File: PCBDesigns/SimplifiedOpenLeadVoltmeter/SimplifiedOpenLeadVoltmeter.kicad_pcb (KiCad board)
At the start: 4 copper layers, 23.9 x 51.3 mm, 33 parts, among them J14 Barrel_Jack, J2 Conn_01x03_Pin, J3 Conn_01x04_MountingPin, J5 Conn_01x03_Pin, Q8 AO3400A MOSFET, U1 ADuM1200AR, U10 LM4040DBZ-2.5, U13 ISO1540, U14 RFM-0505S, U3 ADS1115IDGS

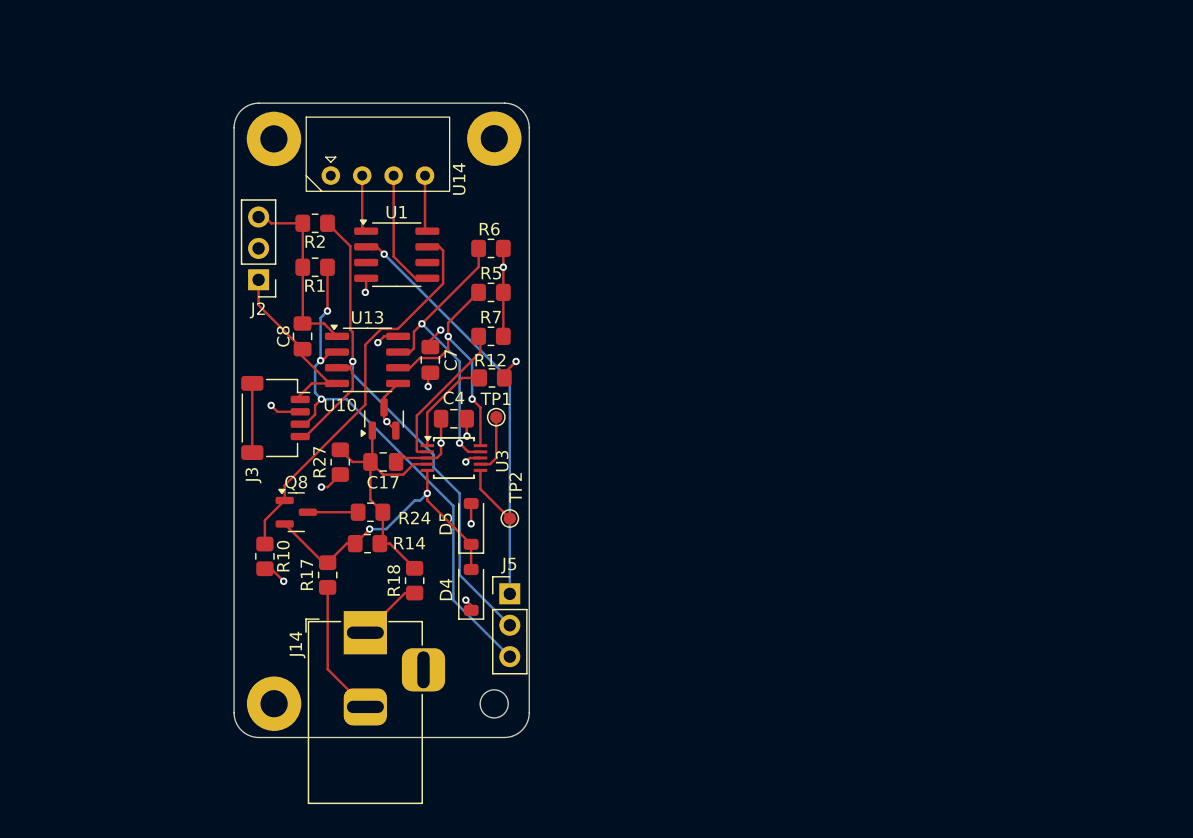
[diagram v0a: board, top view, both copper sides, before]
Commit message: Updates, see description
Updated programming for open lead detect board
worked on various PCBs, including a new open lead voltmeter design with few components
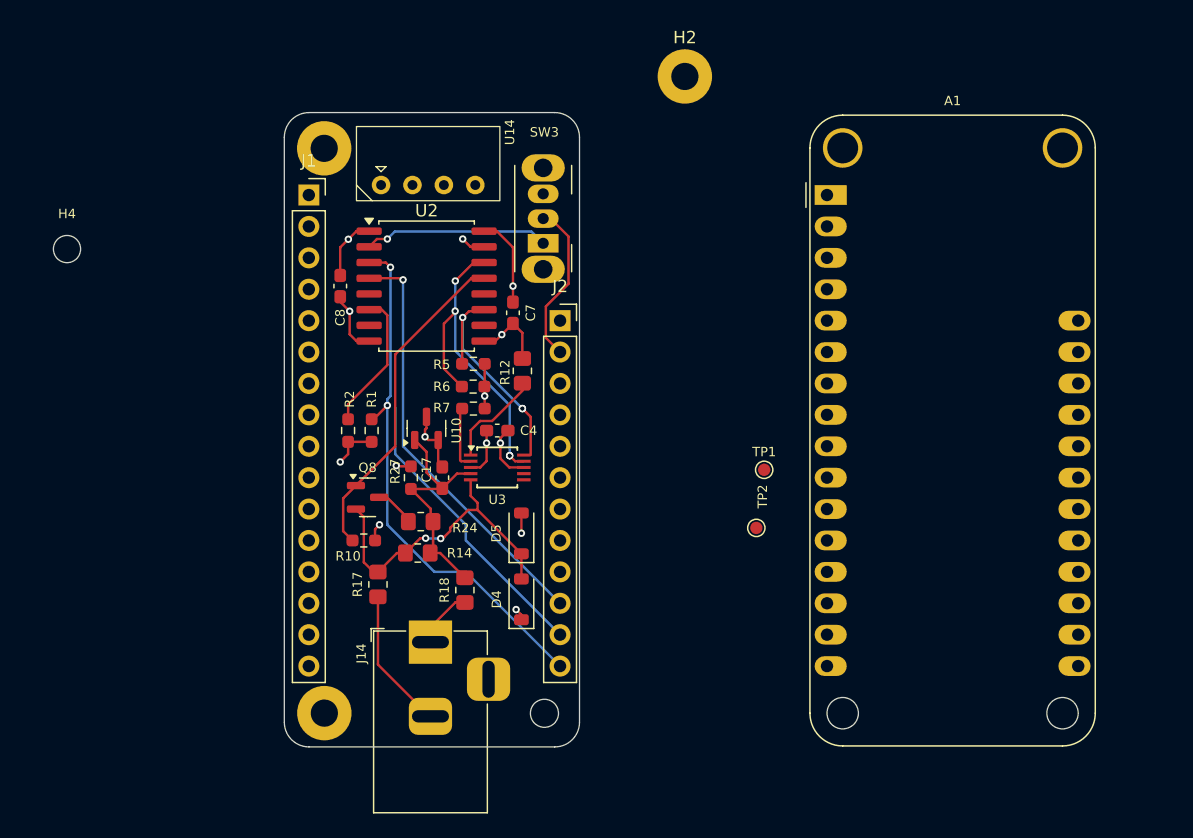
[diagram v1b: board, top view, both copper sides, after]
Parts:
- removed J3: Conn_01x04_MountingPin, Connector_JST:JST_SH_SM04B-SRSS-TB_1x04-1MP_P1.00mm_Horizontal
- removed J5: Conn_01x03_Pin, Connector_PinHeader_2.54mm:PinHeader_1x03_P2.54mm_Vertical
- removed U1: ADuM1200AR, Package_SO:SOIC-8_3.9x4.9mm_P1.27mm
- removed U13: ISO1540, Package_SO:SOIC-8_3.9x4.9mm_P1.27mm
- added A1: Adafruit_Feather_32u4_BluefruitLE, Module:Adafruit_Feather_WithMountingHoles, F.Cu at (194.3, 67.3)
- added H4: MountingHole, MountingHole:MountingHole_2.2mm_M2_ISO14580, F.Cu at (132.8, 71.7)
- added J1: Conn_01x16_Pin, Connector_PinSocket_2.54mm:PinSocket_1x16_P2.54mm_Vertical, F.Cu at (152.4, 67.3)
- added SW3: SW_SPDT, Button_Switch_THT:SW_Slide_SPDT_Angled_CK_OS102011MA1Q, F.Cu at (171.4, 71.2)
- added U2: ISO1644DWR, Package_SO:SOIC-16W_7.5x10.3mm_P1.27mm, F.Cu at (161.9, 74.7)
- C17, C4, C7, C8: footprint Capacitor_SMD:C_0805_2012Metric_Pad1.18x1.45mm_HandSolder -> Capacitor_SMD:C_0603_1608Metric_Pad1.08x0.95mm_HandSolder
- J2: value Conn_01x03_Pin -> Conn_01x12_Pin; footprint Connector_PinHeader_2.54mm:PinHeader_1x03_P2.54mm_Vertical -> Connector_PinSocket_2.54mm:PinSocket_1x12_P2.54mm_Vertical
- R1, R10, R2, R27, R5, R6, R7: footprint Resistor_SMD:R_0805_2012Metric_Pad1.20x1.40mm_HandSolder -> Resistor_SMD:R_0603_1608Metric_Pad0.98x0.95mm_HandSolder
- U14: value RFM-0505S -> DC-DC 0305
- moved J2 24.6 mm to (172.7, 77.5), turned to 0 degrees
- moved TP1 22.1 mm to (189.2, 89.5)
- moved TP2 20.0 mm to (188.6, 94.2)
- moved R2 17.0 mm to (155.6, 86.4), turned to 90 degrees
- moved H2 16.2 mm to (182.8, 57.7)
- moved R1 14.0 mm to (157.5, 86.4), turned to 90 degrees
- moved R6 11.3 mm to (165.7, 82.8)
- moved R10 8.10 mm to (156.8, 95.2), turned to 180 degrees
- moved C7 7.69 mm to (168.9, 76.8)
- moved R7 6.01 mm to (165.7, 84.6)
- moved R5 5.95 mm to (165.7, 81.0)
- moved Q8 5.89 mm to (157.1, 91.8)
- moved R27 5.85 mm to (160.7, 90.2), turned to -90 degrees
- moved J14 5.32 mm to (162.2, 103.5)
- moved C8 5.08 mm to (154.9, 74.7)
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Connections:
- J2 pad 1: GND -> unconnected-(J2-Pin_1-Pad1)
- J2 pad 2: unconnected-(J2-Pin_2-Pad2) -> Net-(A1-EN)
- J2 pad 3: VDD -> unconnected-(J2-Pin_3-Pad3)
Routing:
- net Net-(A1-EN): track 0.00 -> 13.2 mm
- net VDD: track 21.9 -> 8.95 mm, vias 1 -> 2
- net SCL: track 48.3 -> 35.3 mm, vias 1 -> 0
- net Gnd-iso: track 28.0 -> 20.4 mm
- net ADS_ALERT: track 11.8 -> 5.13 mm
- net unconnected-(J3-MountPin-PadMP): track 5.60 -> 0.00 mm
- net /MOSFET_Gate: track 31.9 -> 26.8 mm
- net /AIN2: track 4.88 -> 0.00 mm
- net /AIN3: track 4.79 -> 0.00 mm
- net 5V-iso: track 22.0 -> 17.9 mm, vias 7 -> 5
- net GND: track 16.4 -> 20.1 mm, vias 1 -> 2
- net SDA-5V: track 24.5 -> 27.3 mm, vias 2 -> 4
- net /AIN0: track 21.6 -> 19.8 mm
- net /AIN1: track 24.6 -> 26.1 mm
- net Net-(Q8-D): track 4.06 -> 2.69 mm
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
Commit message: Made circuit boards and BLE circuit boards.
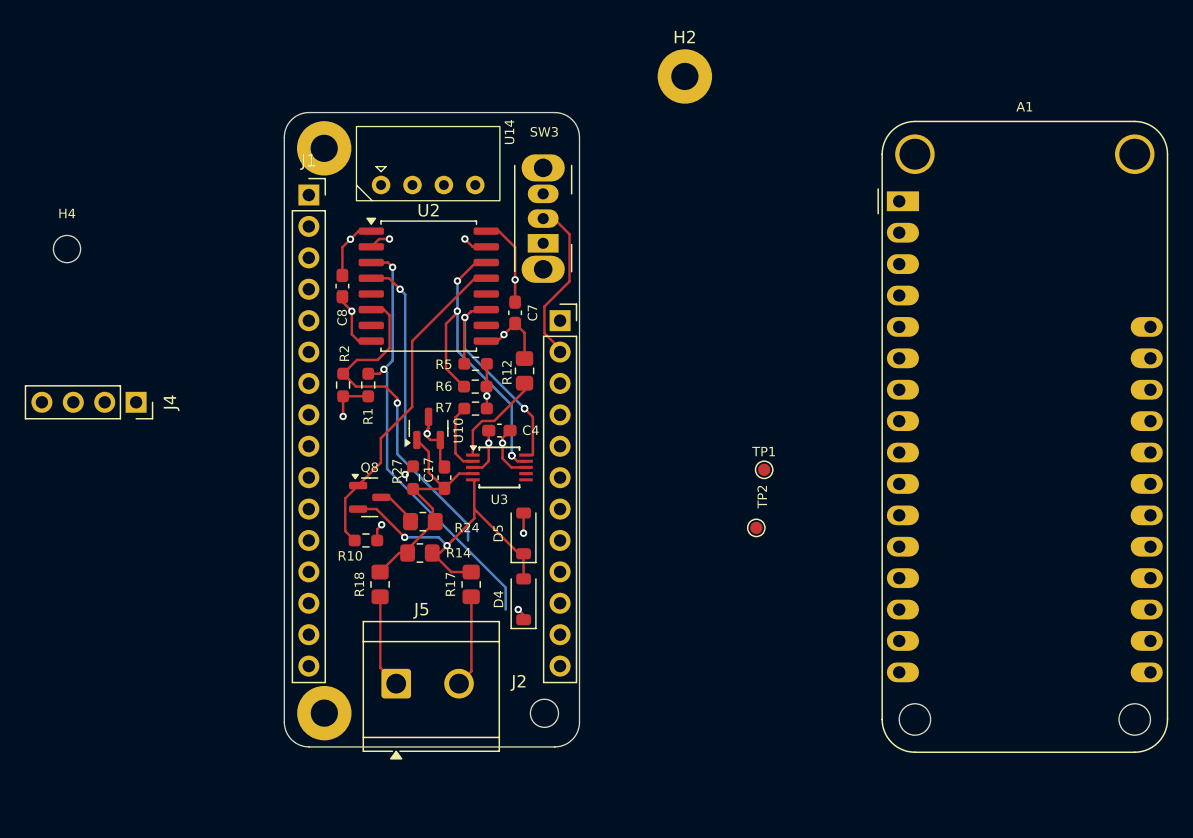
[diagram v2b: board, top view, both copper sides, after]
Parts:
- removed J14: Barrel_Jack, Connector_BarrelJack:BarrelJack_Horizontal
- added J4: Out to Screen, Connector_PinSocket_2.54mm:PinSocket_1x04_P2.54mm_Vertical, F.Cu at (138.4, 84.1)
- added J5: Screw_Terminal_01x02, TerminalBlock_CUI:TerminalBlock_CUI_TB007-508-02_1x02_P5.08mm_Horizontal, F.Cu at (159.5, 106.8)
- moved R17 7.54 mm to (165.5, 98.8)
- moved R18 6.87 mm to (158.2, 98.8)
- moved A1 5.86 mm to (200.2, 67.8)
- moved R2 3.70 mm to (155.2, 82.7)
- moved R1 3.69 mm to (157.2, 82.7)
- moved C17 0.17 mm to (163.4, 90.2)
- moved C4 0.17 mm to (167.8, 86.4)
- moved C7 0.17 mm to (169.1, 76.8)
- moved C8 0.17 mm to (155.1, 74.7)
- moved D4 0.17 mm to (169.8, 100.0)
- moved D5 0.17 mm to (169.8, 94.7)
- moved R10 0.17 mm to (157.0, 95.2)
- moved R12 0.17 mm to (169.8, 81.5)
- moved R14 0.17 mm to (161.4, 96.3), turned to 0 degrees
- moved R24 0.17 mm to (161.6, 93.7)
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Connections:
- R5 pad 1: 5V-iso -> Net-(R5-Pad1)
- R6 pad 1: 5V-iso -> Net-(R5-Pad1)
- R7 pad 1: 5V-iso -> Net-(R5-Pad1)
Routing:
- net /Signal1-MCU: track 34.2 -> 15.6 mm
- net GND: track 20.1 -> 6.89 mm
- net SDA: track 43.5 -> 35.4 mm
- net SCL: track 35.3 -> 28.0 mm, vias 0 -> 1
- net 5V-iso: track 17.9 -> 13.9 mm, vias 5 -> 4
- net V_Input_Float: track 10.9 -> 7.06 mm
- net Net-(R5-Pad1): track 0.00 -> 3.62 mm, vias 0 -> 1
- net V_Input_REF: track 5.32 -> 7.17 mm
- net /AIN1: track 26.1 -> 27.8 mm
